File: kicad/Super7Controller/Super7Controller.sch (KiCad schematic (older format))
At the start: 20 parts, among them P3 CONN_01X13, P4 CONN_01X09, U1 ULN2003A, U2 HiLetgo_ESP-WROOM-32_Developm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

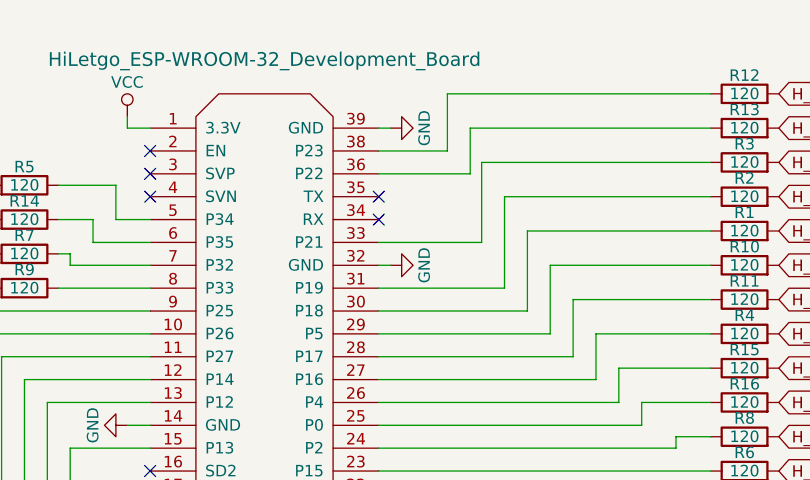
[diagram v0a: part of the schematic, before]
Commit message: only need one ground connection from ESP to ULN
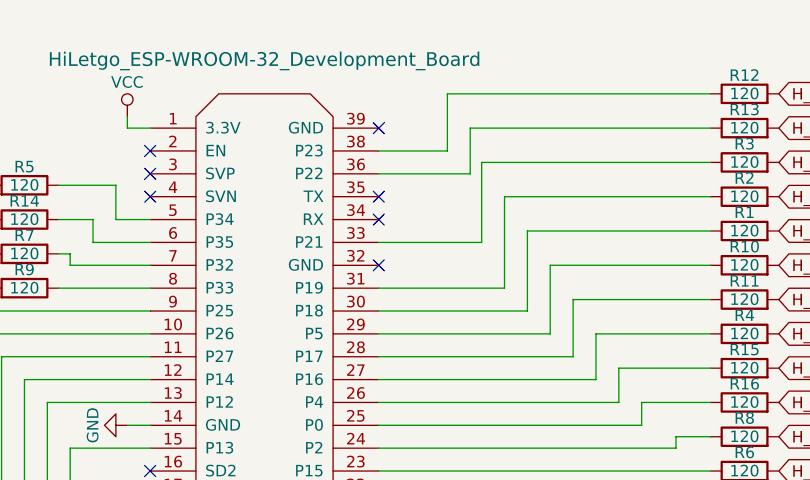
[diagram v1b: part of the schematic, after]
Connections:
- net GND: no longer U2.32 (GND), U2.39 (GND)
- no-connect marks 15 -> 17
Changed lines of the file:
@@
 Wire Wire Line
 	6700 1650 6700 1600
-$Comp
-L GND #PWR07
-U 1 1 5A71E497
-P 7850 1650
-F 0 "#PWR07" H 7850 1400 50  0001 C CNN
-F 1 "GND" H 7850 1500 50  0000 C CNN
-F 2 "" H 7850 1650 50  0000 C CNN
-F 3 "" H 7850 1650 50  0000 C CNN
-	1    7850 1650
-	0    -1   -1   0
-$EndComp
-$Comp
-L GND #PWR08
-U 1 1 5A71E4E1
-P 7850 2250
-F 0 "#PWR08" H 7850 2000 50  0001 C CNN
-F 1 "GND" H 7850 2100 50  0000 C CNN
-F 2 "" H 7850 2250 50  0000 C CNN
-F 3 "" H 7850 2250 50  0000 C CNN
-	1    7850 2250
-	0    -1   -1   0
-$EndComp
 Wire Wire Line
 	6800 2950 6700 2950
-Wire Wire Line
-	7850 2250 7800 2250
-Wire Wire Line
-	7850 1650 7800 1650
 Wire Wire Line
 	8100 1500 8100 1750
@@
 NoConn ~ 6800 3250
 NoConn ~ 6800 3150
+NoConn ~ 7800 2250
+NoConn ~ 7800 1650
 $EndSCHEMATC

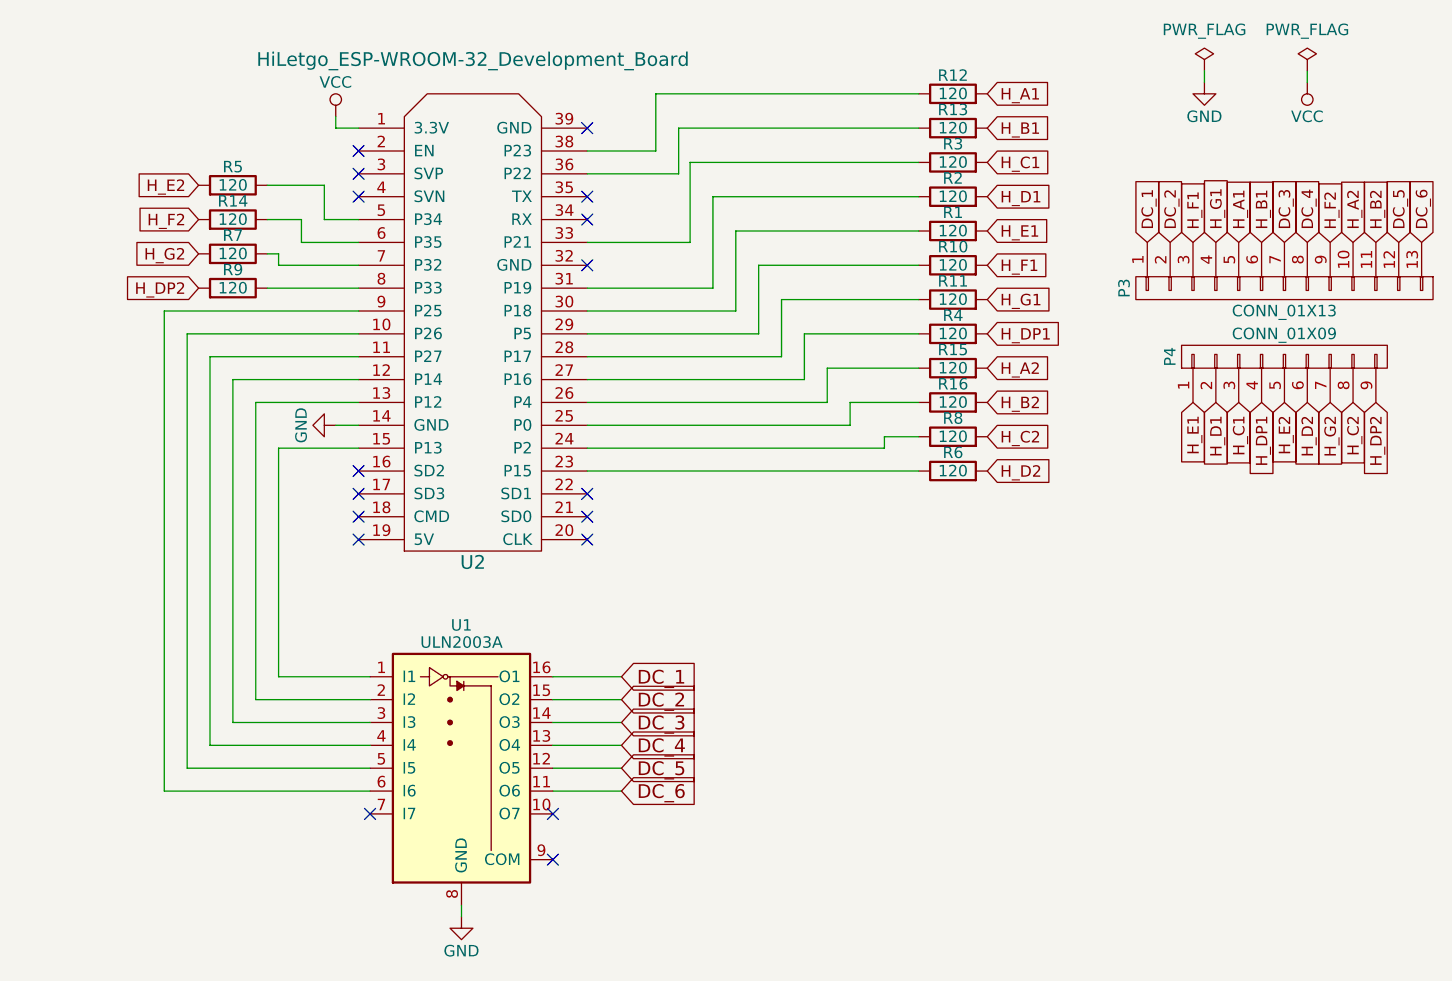
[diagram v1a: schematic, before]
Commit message: reroute lines to match autorouter
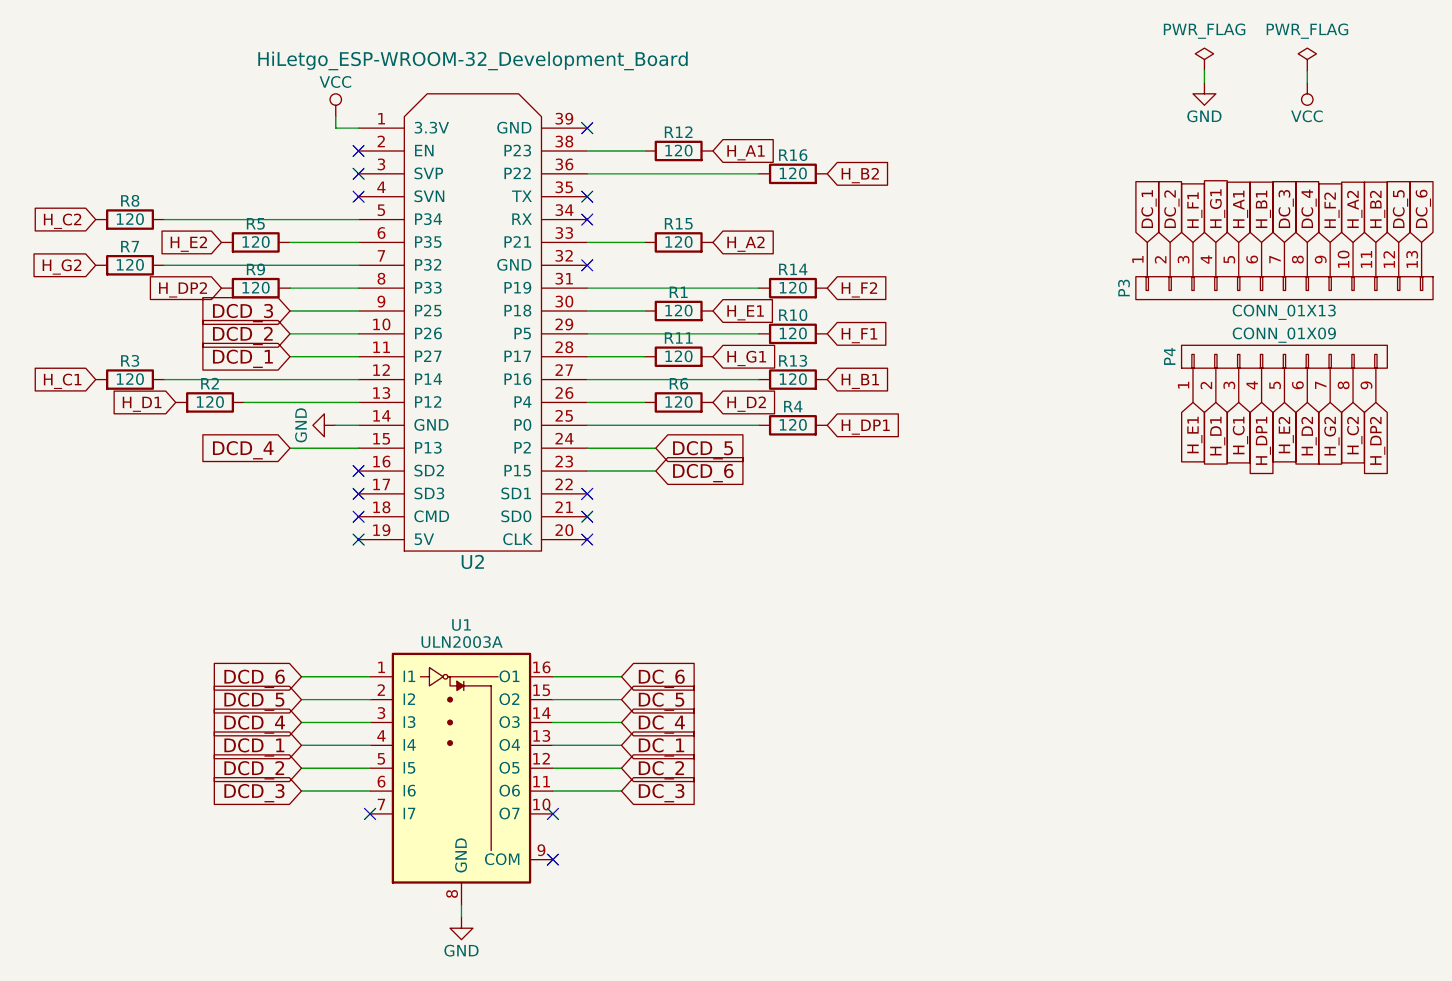
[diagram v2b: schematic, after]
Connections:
- net DC_1: now also U1.13 (O4); no longer U1.16 (O1)
- net DC_2: now also U1.12 (O5); no longer U1.15 (O2)
- net DC_3: now also U1.11 (O6); no longer U1.14 (O3)
- net DC_4: now also U1.14 (O3); no longer U1.13 (O4)
- net DC_5: now also U1.15 (O2); no longer U1.12 (O5)
- net DC_6: now also U1.16 (O1); no longer U1.11 (O6)
- net at R13.1: now also U2.27 (P16); no longer U2.36 (P22)
- net at R3.1: now also U2.12 (P14); no longer U2.33 (P21)
- net at R2.1: now also U2.13 (P12); no longer U2.31 (P19)
- net at R4.1: now also U2.25 (P0); no longer U2.27 (P16)
- net at R15.1: now also U2.33 (P21); no longer U2.26 (P4)
- net at R16.1: now also U2.36 (P22); no longer U2.25 (P0)
- net at R8.1: now also U2.5 (P34); no longer U2.24 (P2)
- net at R6.1: now also U2.26 (P4); no longer U2.23 (P15)
- net at R5.1: now also U2.6 (P35); no longer U2.5 (P34)
- net at R14.1: now also U2.31 (P19); no longer U2.6 (P35)
- net DCD_2: now reaches U1.5 (I5), U2.10 (P26)
- net DCD_1: now reaches U1.4 (I4), U2.11 (P27)
- net DCD_4: now reaches U1.3 (I3)
- net DCD_4: now also U2.15 (P13); no longer U2.12 (P14)
- net DCD_5: now reaches U1.2 (I2)
- net DCD_5: now also U2.24 (P2); no longer U2.13 (P12)
- net DCD_6: now reaches U1.1 (I1)
- net DCD_6: now also U2.23 (P15); no longer U2.15 (P13)
- net DCD_3: now reaches U1.6 (I6), U2.9 (P25)
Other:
- moved on the sheet: R1, R10, R11, R12, R13, R14, R15, R16, R2, R3, R4, R5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

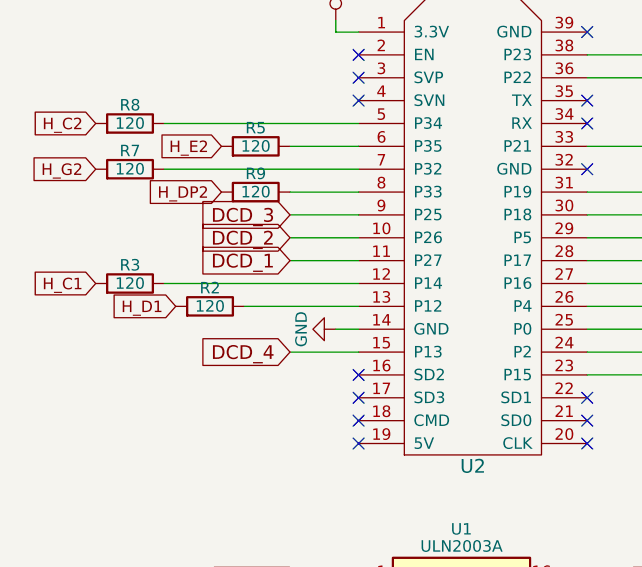
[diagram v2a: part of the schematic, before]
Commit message: correct errors in netlist
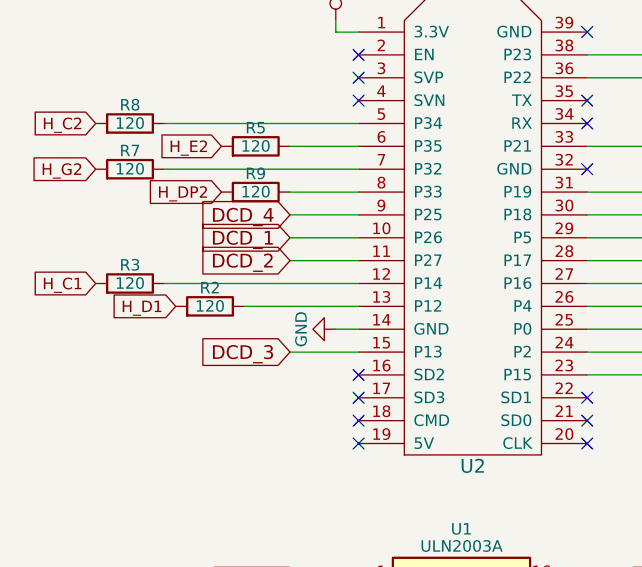
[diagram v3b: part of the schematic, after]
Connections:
- net DCD_1: now also U2.10 (P26); no longer U2.11 (P27)
- net DCD_2: now also U2.11 (P27); no longer U2.10 (P26)
- net DCD_3: now also U2.15 (P13); no longer U2.9 (P25)
- net DCD_4: now also U2.9 (P25); no longer U2.15 (P13)
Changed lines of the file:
@@
 $EndComp
 $Comp
-L GND #PWR09
+L GND #PWR07
 U 1 1 5A722BDF
 P 7250 5100
-F 0 "#PWR09" H 7250 4850 50  0001 C CNN
+F 0 "#PWR07" H 7250 4850 50  0001 C CNN
 F 1 "GND" H 7250 4950 50  0000 C CNN
 F 2 "" H 7250 5100 50  0000 C CNN
@@
 	7800 3050 8100 3050
 Text GLabel 6500 3050 0    60   Input ~ 0
-DCD_4
+DCD_3
 Wire Wire Line
 	6800 3050 6500 3050
 Text GLabel 6500 2650 0    60   Input ~ 0
-DCD_1
+DCD_2
 Wire Wire Line
 	6500 2650 6800 2650
 Text GLabel 6500 2550 0    60   Input ~ 0
-DCD_2
+DCD_1
 Text GLabel 6500 2450 0    60   Input ~ 0
-DCD_3
+DCD_4
 Wire Wire Line
 	6500 2450 6800 2450

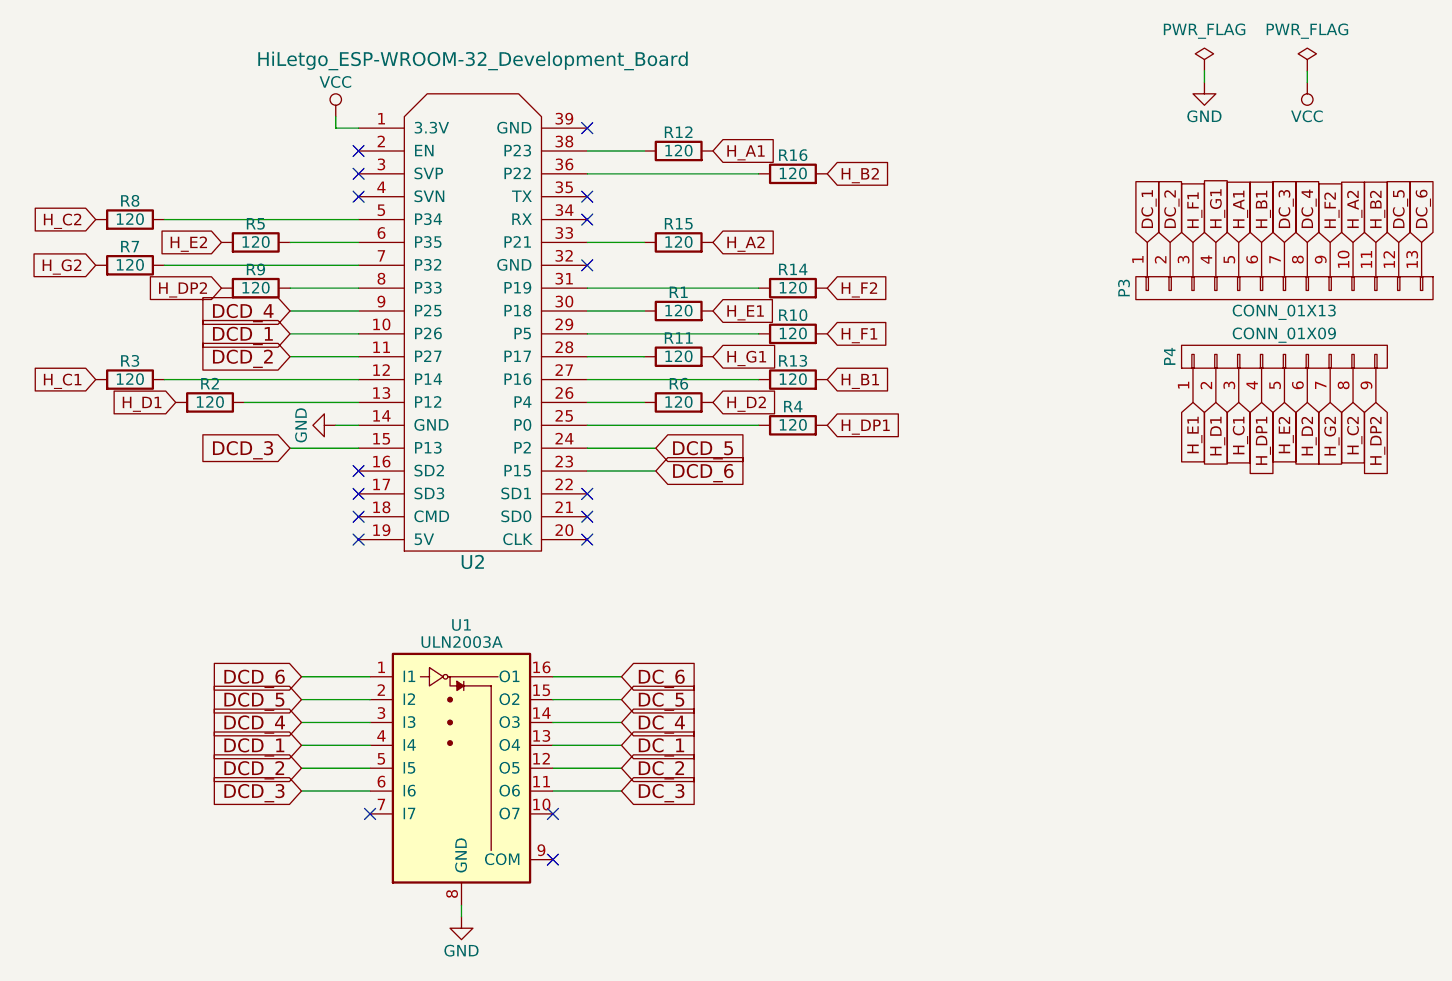
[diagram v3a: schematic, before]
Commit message: move resistor connections to make routing easier
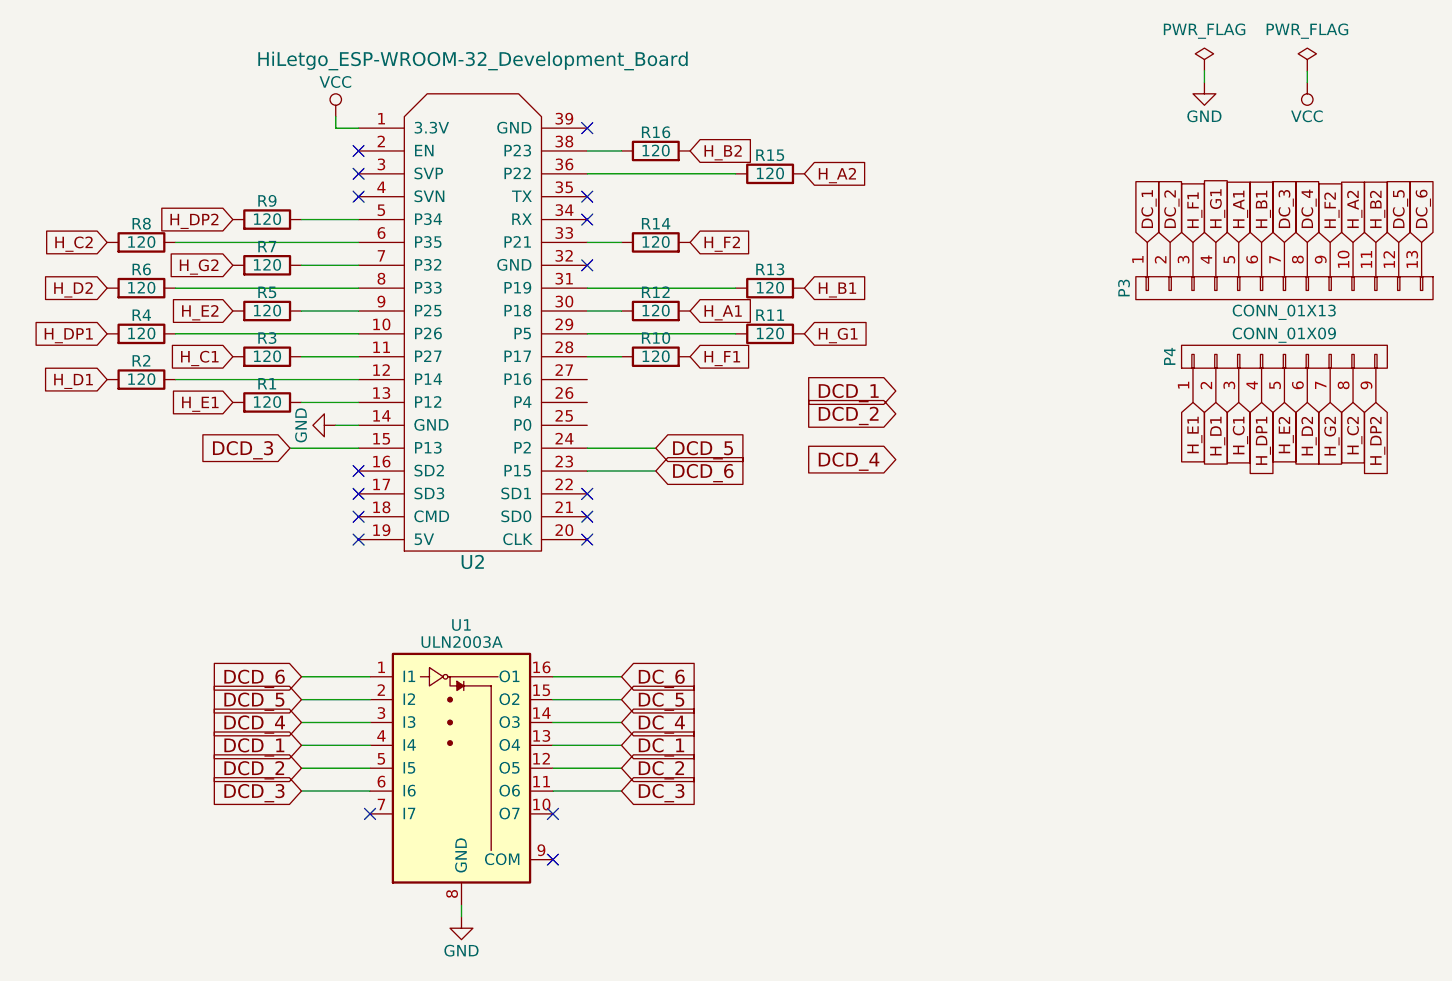
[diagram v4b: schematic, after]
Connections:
- net DCD_1: no longer U2.10 (P26)
- net DCD_2: no longer U2.11 (P27)
- net DCD_4: no longer U2.9 (P25)
- net at R12.1: now also U2.30 (P18); no longer U2.38 (P23)
- net at R13.1: now also U2.31 (P19); no longer U2.27 (P16)
- net at R3.1: now also U2.11 (P27); no longer U2.12 (P14)
- net at R2.1: now also U2.12 (P14); no longer U2.13 (P12)
- net at R1.1: now also U2.13 (P12); no longer U2.30 (P18)
- net at R10.1: now also U2.28 (P17); no longer U2.29 (P5)
- net at R11.1: now also U2.29 (P5); no longer U2.28 (P17)
- net at R4.1: now also U2.10 (P26); no longer U2.25 (P0)
- net at R15.1: now also U2.36 (P22); no longer U2.33 (P21)
- net at R16.1: now also U2.38 (P23); no longer U2.36 (P22)
- net at R8.1: now also U2.6 (P35); no longer U2.5 (P34)
- net at R6.1: now also U2.8 (P33); no longer U2.26 (P4)
- net at R5.1: now also U2.9 (P25); no longer U2.6 (P35)
- net at R14.1: now also U2.33 (P21); no longer U2.31 (P19)
- net at R9.1: now also U2.5 (P34); no longer U2.8 (P33)
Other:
- moved on the sheet: R1, R10, R11, R12, R13, R14, R15, R16, R2, R3, R4, R5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
